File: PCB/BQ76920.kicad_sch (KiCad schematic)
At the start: 81 parts, among them CN6 WAFER-SH1.0-6PWB, Q1 CSD13381F4, Q10 TP0610K-T1-GE3, Q2 CSD13381F4, Q3 CSD13381F4, Q4 CSD13381F4, Q5 CSD13381F4, Q6 BSC0702LS, Q7 BSC0702LS, Q8 BSC0702LS, Q9 BSC0702LS, SW3 B3U-1000P, U3 TPS61240DRVR, U4 BQ7692003PW

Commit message: Signed-off-by: jasperThinkpad <2567434944@qq.com>
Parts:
- renumbered C20 to C10, C28 to C11, C16 to C12, C9 to C13, C10 to C14, C24 to C15, C18 to C16, C11 to C17, C15 to C18, C17 to C19, C19 to C20, C12 to C21, C13 to C22, C21 to C23, C22 to C24, C23 to C25, C14 to C26, C25 to C27, C26 to C28, C27 to C9, CN6 to CN7, D7 to D10, D12 to D11, D8 to D12, D9 to D4, D10 to D5, D4 to D6, D5 to D7, D6 to D8, D11 to D9, H7 to H6, H6 to H7, Q9 to Q10, Q10 to Q4, Q4 to Q5, Q5 to Q6, Q6 to Q7, Q7 to Q9, R37 to R11, R17 to R12, R12 to R13, R18 to R14, R19 to R15, R13 to R16, R38 to R17, R20 to R18, R29 to R19, R28 to R20, R14 to R22, R30 to R23, R22 to R24, R23 to R25, R15 to R26, R24 to R27, R39 to R28, R25 to R29, R16 to R30, R26 to R31, R40 to R32, R31 to R33, R35 to R34, R36 to R35, R32 to R36, R27 to R37, R33 to R38, R34 to R39
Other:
- moved on the sheet: C10, C11, C12, C9, D4, D5, H5, H6, H7, H8, L2, R11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

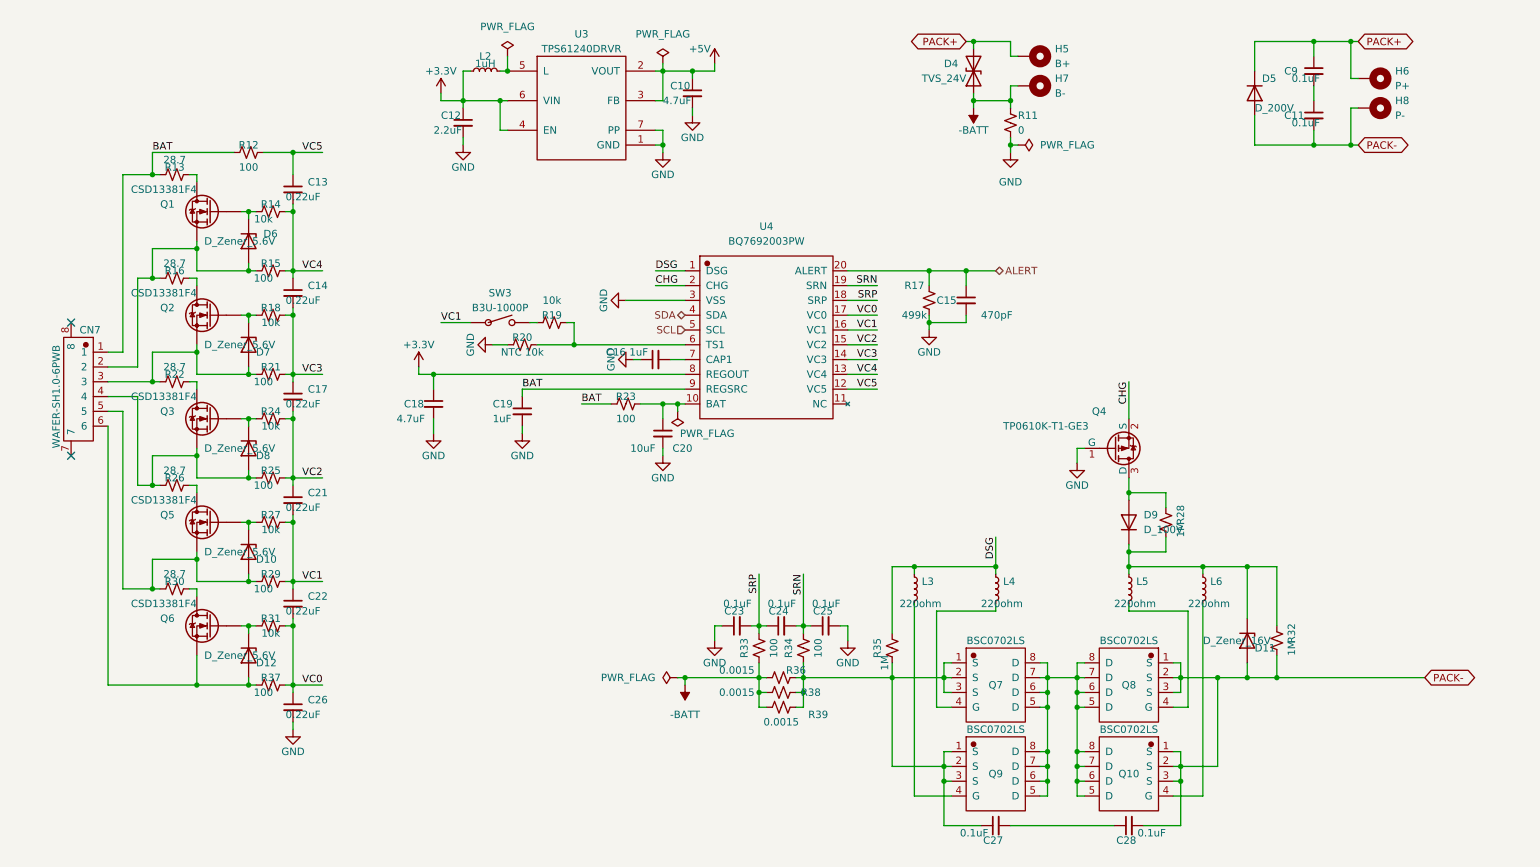
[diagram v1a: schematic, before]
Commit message: 3.5 布局完成
Signed-off-by: jasper <2567434944@qq.com>
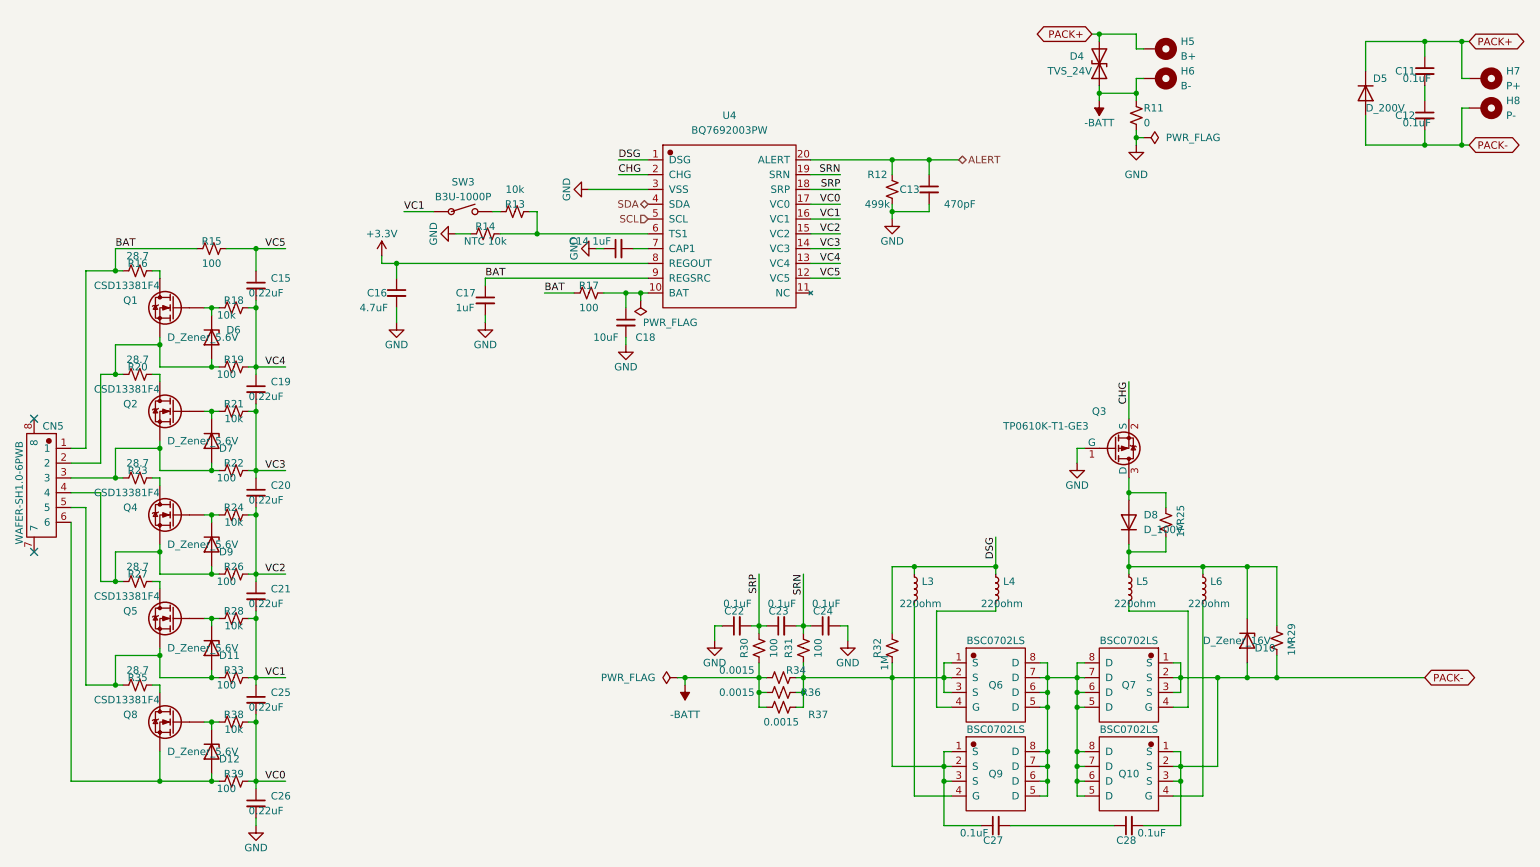
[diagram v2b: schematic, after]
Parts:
- removed C10: 4.7uF, Capacitor_SMD:C_0402_1005Metric_Pad0.74x0.62mm_HandSolder, symbol Device:C_Small
- removed C12: 2.2uF, Capacitor_SMD:C_0402_1005Metric_Pad0.74x0.62mm_HandSolder, symbol Device:C_Small
- removed L2: 1uH, Inductor_SMD:L_1210_3225Metric_Pad1.42x2.65mm_HandSolder, symbol Device:L_Small
- removed U3: TPS61240DRVR, Rick_DC-DC:TPS61240DRVR_WSON-6_L2.0-W2.0-P0.65-TL-EP, symbol Rick_DC-DC:TPS61240DRVR
- renumbered C9 to C11, C11 to C12, C15 to C13, C16 to C14, C13 to C15, C18 to C16, C19 to C17, C20 to C18, C14 to C19, C17 to C20, C23 to C22, C24 to C23, C25 to C24, C22 to C25, CN7 to CN5, D11 to D10, D10 to D11, D9 to D8, D8 to D9, H7 to H6, H6 to H7, Q4 to Q3, Q3 to Q4, Q7 to Q6, Q8 to Q7, Q6 to Q8, R17 to R12, R19 to R13, R20 to R14, R12 to R15, R13 to R16, R23 to R17, R14 to R18, R15 to R19, R16 to R20, R18 to R21, R21 to R22, R22 to R23, R28 to R25, R25 to R26, R26 to R27, R27 to R28, R32 to R29, R33 to R30, R34 to R31, R35 to R32, R29 to R33, R36 to R34, R30 to R35, R38 to R36, R39 to R37, R31 to R38, R37 to R39
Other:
- moved on the sheet: C11, C12, C13, C14, C15, C16, C17, C18, C19, C20, C21, C25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
